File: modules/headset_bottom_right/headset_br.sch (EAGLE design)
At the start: 287 parts, among them U1 CDCLVC1103, U2 2N7002, U3 2N7002, U300 ADAU1701/02ADAU1701JSTZ, U4 2N7002, U400 PGA2505, U5 2N7002, U500 PCM4202, U600 PCM1791A, U700 TPA6130A2, X1 JTAG, X200 8MHz, X400 NCJ10FI-H-0, X700 NMJ6HHD2

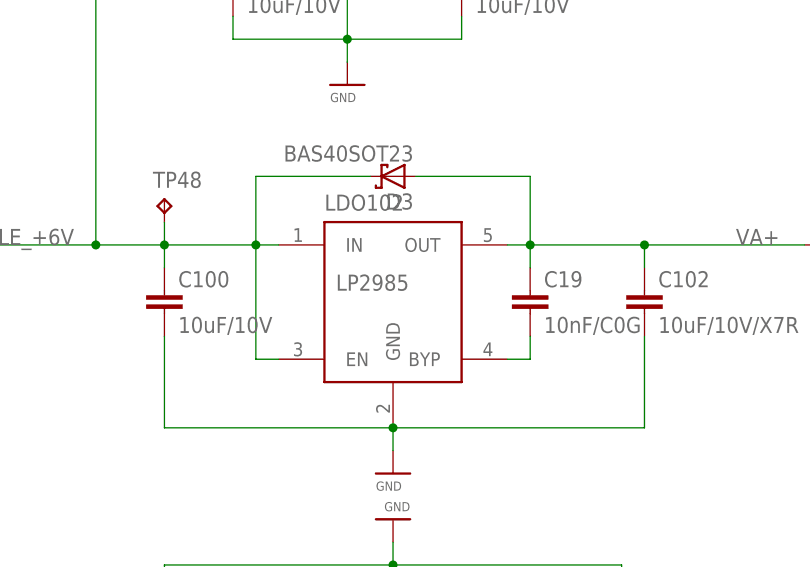
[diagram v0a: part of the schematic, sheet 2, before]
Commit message: added attributes to build a usable BOM
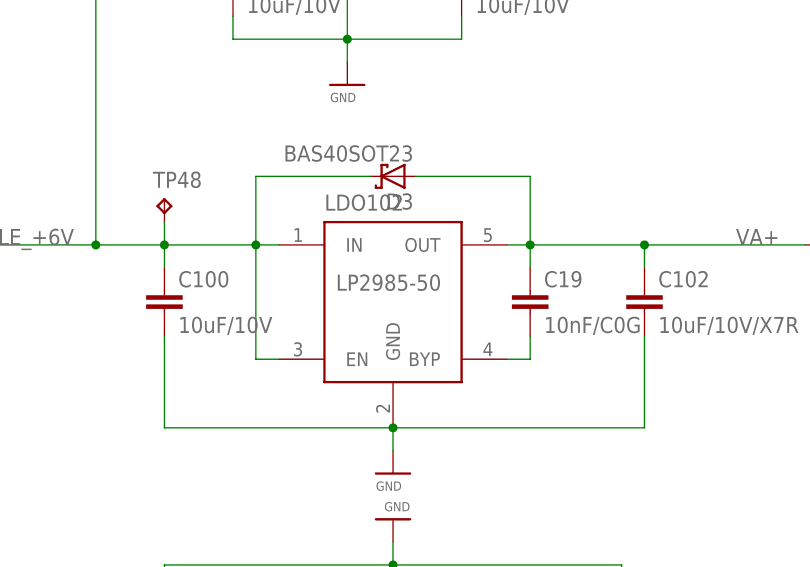
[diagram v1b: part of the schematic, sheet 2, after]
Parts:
- C1, C2, C6, C7: OC_DIGIKEY (none) -> 311-1355-1-ND; OC_FARNELL (none) -> 9402144
- C100, C102, C104, C18, C206, C3, C32: MANUFACTURER (none) -> TDK; MPN (none) -> C2012X7R1A106K125AC; OC_DIGIKEY (none) -> 445-6857-1-ND; OC_FARNELL (none) -> 2346934; OC_MOUSER (none) -> 810-C2012X7R1A106K
- C1000, C400, C401, C8, C9, C916, C917, C918: MANUFACTURER (none) -> TDK; MPN (none) -> C1608X7R1C105K080AC; OC_DIGIKEY (none) -> 445-1604-1-ND; OC_FARNELL (none) -> 1907343; OC_MOUSER (none) -> 810-C1608X7R1C105K
- C11, C20, C200, C201, C202, C203, C204, C205, C21, C300, C301, C302, C303, C304, C305, C306, C307, C308, C40, C402, C403, C404, C405, C406, C42, C43, C44, C500, C501, C502, C503: MANUFACTURER (none) -> AVX; MPN (none) -> 0603YC104KAT2A; OC_DIGIKEY (none) -> 478-1239-1-ND; OC_FARNELL (none) -> 1327679; OC_MOUSER (none) -> 581-060316C104K
- C17, C19, C31: MANUFACTURER (none) -> TDK; MPN (none) -> C1608C0G1H103J080AA; OC_DIGIKEY (none) -> 445-7404-1-ND; OC_FARNELL (none) -> 1907314; OC_MOUSER (none) -> 810-C1608C0G1H103J
- C207, C208: MANUFACTURER (none) -> Kemet; MPN (none) -> C0603C180J5GACTU; OC_DIGIKEY (none) -> 399-1052-1-ND; OC_FARNELL (none) -> 1414620; OC_MOUSER (none) -> 80-C0603C180J5G
- C22, C309, C310, C311: MANUFACTURER (none) -> Kemet; MPN (none) -> C1206C106K4RACTU; OC_DIGIKEY (none) -> 399-3525-1-ND; OC_FARNELL (none) -> 2392400; OC_MOUSER (none) -> 80-C1206C106K4R
- C23, C24, C28: MANUFACTURER (none) -> TDK; MPN (none) -> CGA3E1X7R1C474K080AC; OC_DIGIKEY (none) -> 445-5672-1-ND; OC_FARNELL (none) -> 2210843; OC_MOUSER (none) -> 810-CGA3E1X7R1C474K
- C25: MANUFACTURER (none) -> TDK; MPN (none) -> C0603C0G1H470J030BA; OC_DIGIKEY (none) -> 445-1782-1-ND; OC_MOUSER (none) -> 810-C0603C0G1H470J
- C26, C27: MANUFACTURER (none) -> Panasonic; MPN (none) -> EEE-FK1E470P; OC_DIGIKEY (none) -> PCE3804CT-ND; OC_FARNELL (none) -> 9695753; OC_MOUSER (none) -> 667-EEE-FK1E470P
- C29, C30: MANUFACTURER (none) -> Murata; MPN (none) -> GRM31CR61H106KA12L; OC_DIGIKEY (none) -> 490-5961-1-ND; OC_FARNELL (none) -> 1845762; OC_MOUSER (none) -> 81-GRM31CR61H106KA2L
- C312: MANUFACTURER (none) -> Kemet; MPN (none) -> C0603C332K5RACTU; OC_DIGIKEY (none) -> 399-1086-1-ND; OC_FARNELL (none) -> 1414635; OC_MOUSER (none) -> 80-C0603C332K5R
- C313: MANUFACTURER (none) -> Vishay; MPN (none) -> VJ0603Y563KXJPW1BC; OC_MOUSER (none) -> 77-VJ0603Y563KXJPBC
- C39, C41: MANUFACTURER (none) -> AVX; MPN (none) -> F931A106KAA; OC_DIGIKEY (none) -> 478-8192-1-ND; OC_MOUSER (none) -> 647-F931A106KAA
- C4, C411, C412, C413: MANUFACTURER (none) -> AVX; MPN (none) -> TAJB475K020RNJ; OC_DIGIKEY (none) -> 478-3887-1-ND; OC_FARNELL (none) -> 197403; OC_MOUSER (none) -> 581-TAJB475K020
- C407: MANUFACTURER (none) -> Murata; MPN (none) -> GRM033R61A272KA01D; OC_DIGIKEY (none) -> 490-6141-1-ND; OC_MOUSER (none) -> 81-GRM033R61A272KA1D
- C408, C409, C416, C417: MANUFACTURER (none) -> AVX; MPN (none) -> 06035A101JAT2A; OC_DIGIKEY (none) -> 478-1175-1-ND; OC_FARNELL (none) -> 499122; OC_MOUSER (none) -> 581-06035A101J
- C414, C415: MANUFACTURER (none) -> Panasonic; MPN (none) -> EEEFK1J470P; OC_DIGIKEY (none) -> PCE3823CT-ND; OC_FARNELL (none) -> 9696032; OC_MOUSER (none) -> EEE-FK1J470P
- C504: MANUFACTURER (none) -> Vishay; MPN (none) -> TR3B476K010C0350; OC_DIGIKEY (none) -> 718-1768-1-ND; OC_FARNELL (none) -> 74-TR3B476K010C0350
- C505, C506: MANUFACTURER (none) -> Kemet; MPN (none) -> EDK476M010A9DAA; OC_FARNELL (none) -> 2068642
- C900, C908, C910, C911: MANUFACTURER (none) -> Kemet; MPN (none) -> C0603C221J5GACTU; OC_FARNELL (none) -> 1414623; OC_MOUSER (none) -> 80-C0603C221J5G
- C904, C905, C906, C907, C919: MANUFACTURER (none) -> TDK; MPN (none) -> C1608X7R1A225K080AC; OC_DIGIKEY (none) -> 445-5958-1-ND; OC_FARNELL (none) -> 2346896; OC_MOUSER (none) -> 810-C1608X7R1A225K
- D400, D401: MANUFACTURER (none) -> Vishay; MPN (none) -> BZG05C5V6TR; OC_DIGIKEY (none) -> BZG05C5V6CT-ND; OC_FARNELL (none) -> 1612397; OC_MOUSER (none) -> 78-BZG05C5V6
- LDO100: OC_DIGIKEY (none) -> MCP1702T-3302E/CBCT-ND; OC_FARNELL (none) -> 1331490; OC_MOUSER (none) -> 579-MCP1702T3302E/CB
- LDO101: MANUFACTURER (none) -> Microchip; MPN (none) -> MCP1702T-5002E/CB; OC_DIGIKEY (none) -> MCP1702T-5002E/CBCT-ND; OC_FARNELL (none) -> 1331491; OC_MOUSER (none) -> 579-MCP1702T5002E/CB
- LDO102: value LP2985 -> LP2985-50; MPN (none) -> LP2985-50DBVR; OC_DIGIKEY (none) -> 296-20717-1-ND; OC_FARNELL (none) -> 2008643; OC_MOUSER (none) -> 595-LP2985-50DBVR
- LDO103: MPN (none) -> LT1964ES5-5#TRMPBF; OC_DIGIKEY (none) -> LT1964ES5-5#TRMPBFCT-ND; OC_FARNELL (none) -> 1663814
- LDO104: MANUFACTURER (none) -> Microchip; MPN (none) -> MCP1702T-1802E/CB; OC_DIGIKEY (none) -> MCP1702T-1802E/CBCT-ND; OC_FARNELL (none) -> 1331488; OC_MOUSER (none) -> 579-MCP1702T1802E/CB
- R1, R201, R312, R39, R924: MANUFACTURER (none) -> Vishay; MPN (none) -> CRCW06031K00FKEA; OC_DIGIKEY (none) -> 541-1.00KHCT-ND; OC_FARNELL (none) -> 1469740; OC_MOUSER (none) -> 71-CRCW0603-1.0K-E3
- R1001, R1002, R1003: MANUFACTURER (none) -> Panasonic; MPN (none) -> ERJ-3EKF22R0V; OC_DIGIKEY (none) -> P22.0HCT-ND; OC_FARNELL (none) -> 2346653; OC_MOUSER (none) -> 667-ERJ-3EKF22R0V
- R11, R12, R15, R16, R2, R20, R200, R204, R205, R21, R22, R3, R505, R65, R67, R912: MANUFACTURER (none) -> Panasonic; MPN (none) -> ERJ-3EKF1002V; OC_DIGIKEY (none) -> P10.0KHCT-ND; OC_FARNELL (none) -> 1987593; OC_MOUSER (none) -> 667-ERJ-3EKF1002V
- R17, R18, R19, R24, R25, R27, R32, R33, R41, R410, R411, R412, R413, R42, R43, R44, R45, R46, R47, R48, R49, R50, R51, R512, R513, R514, R515, R52, R913, R914, R915: MANUFACTURER (none) -> Panasonic; MPN (none) -> ERJ-3EKF1000V; OC_DIGIKEY (none) -> P100HCT-ND; OC_FARNELL (none) -> 2303059; OC_MOUSER (none) -> 667-ERJ-3EKF1000V
- R202, R203: MANUFACTURER (none) -> Panasonic; MPN (none) -> ERJ-3EKF4701V; OC_DIGIKEY (none) -> P4.70KHCT-ND; OC_FARNELL (none) -> 2304687; OC_MOUSER (none) -> 667-ERJ-3EKF4701V
- R300: MANUFACTURER (none) -> Panasonic; MPN (none) -> ERJ-3EKF4750V; OC_DIGIKEY (none) -> P475HCT-ND; OC_FARNELL (none) -> 2059310; OC_MOUSER (none) -> 667-ERJ-3EKF4750V
- R37: value 480R -> 475R; MANUFACTURER (none) -> Panasonic; MPN (none) -> ERJ-3EKF4750V; OC_DIGIKEY (none) -> P475HCT-ND; OC_FARNELL (none) -> 2059310; OC_MOUSER (none) -> 667-ERJ-3EKF4750V
- R400, R405, R406: MANUFACTURER (none) -> Bourns; MPN (none) -> CRT1206-BY-10R0ELF; OC_DIGIKEY (none) -> CRT1206-BY-10R0ELFCT-ND; OC_FARNELL (none) -> 2008318; OC_MOUSER (none) -> 652-CRT1206BY10R0ELF
- R401, R402: MANUFACTURER (none) -> Vishay; MPN (none) -> PHP00805E40R2BST1; OC_MOUSER (none) -> 71-PHP00805E40R2BST1
- R407, R408: MANUFACTURER (none) -> Vishay; MPN (none) -> TNPW12066K81BEEN; OC_DIGIKEY (none) -> TNPW12066K81BEEN-ND; OC_MOUSER (none) -> 71-TNPW12066K81BEEN
- R54, R55: MANUFACTURER (none) -> Panasonic; MPN (none) -> ERJ-3EKF4702V; OC_DIGIKEY (none) -> P47.0KHCT-ND; OC_FARNELL (none) -> 1991766; OC_MOUSER (none) -> 667-ERJ-3EKF4702V
- R56, R57: MANUFACTURER (none) -> Vishay; MPN (none) -> TNPW12069K09BEEA; OC_DIGIKEY (none) -> TNP9.09KACCT-ND; OC_MOUSER (none) -> 71-TNPW12069K09BEEA
- R58, R59: MANUFACTURER (none) -> Panasonic; MPN (none) -> ERJ-8ENF1101V; OC_DIGIKEY (none) -> P1.10KFCT-ND; OC_FARNELL (none) -> 2283515; OC_MOUSER (none) -> 667-ERJ-8ENF1101V
- R60: MANUFACTURER (none) -> Panasonic; MPN (none) -> ERJ-8ENF2670V; OC_DIGIKEY (none) -> P267FCT-ND; OC_FARNELL (none) -> 2359456; OC_MOUSER (none) -> 667-ERJ-8ENF2670V
- R61, R62: MANUFACTURER (none) -> Panasonic; MPN (none) -> ERA-6AEB1211V; OC_DIGIKEY (none) -> P1.21KDACT-ND; OC_MOUSER (none) -> 667-ERA-6AEB1211V
- R63: MANUFACTURER (none) -> Panasonic; MPN (none) -> ERJ-3EKF4422V; OC_DIGIKEY (none) -> P44.2KHCT-ND; OC_FARNELL (none) -> 2059467; OC_MOUSER (none) -> 667-ERJ-3EKF4422V
- R64: MANUFACTURER (none) -> Panasonic; MPN (none) -> ERJ-3EKF1101V; OC_DIGIKEY (none) -> P1.10KHCT-ND; OC_FARNELL (none) -> 2059329; OC_MOUSER (none) -> 667-ERJ-3EKF1101V
- R900, R901, R902, R903: MANUFACTURER (none) -> Panasonic; MPN (none) -> ERJ-3EKF2002V; OC_DIGIKEY (none) -> P20.0KHCT-ND; OC_FARNELL (none) -> 2059432; OC_MOUSER (none) -> 667-ERJ-3EKF2002V
- UC200: MANUFACTURER (none) -> ST; MPN (none) -> STM32F100C8T6B; OC_DIGIKEY (none) -> 497-10499-ND; OC_FARNELL (none) -> 1838511; OC_MOUSER (none) -> 511-STM32F100C8T6B
- X200: MPN (none) -> ABM7-8.000MHZ-D2Y-T; OC_DIGIKEY (none) -> 535-9831-1-ND; OC_FARNELL (none) -> 2101337; OC_MOUSER (none) -> 815-ABM7-8-D2Y-T
- X400: MANUFACTURER (none) -> Neutrik; OC_MOUSER (none) -> 568-NCJ10FI-H-0
- X700: OC_MOUSER (none) -> 550-25382
